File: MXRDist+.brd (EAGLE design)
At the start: 100 x 80 mm, 31 parts, among them IC1 LM741P

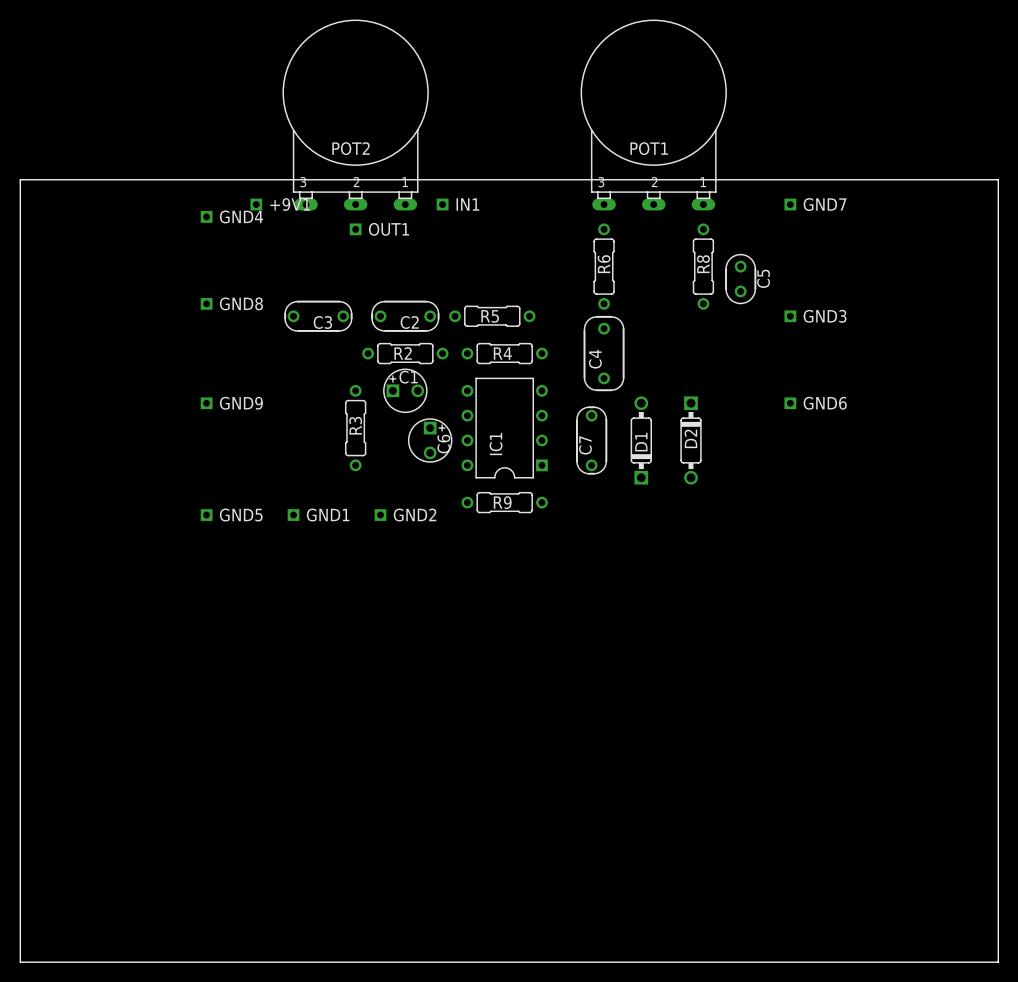
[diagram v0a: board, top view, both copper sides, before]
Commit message: New layout with diode switch
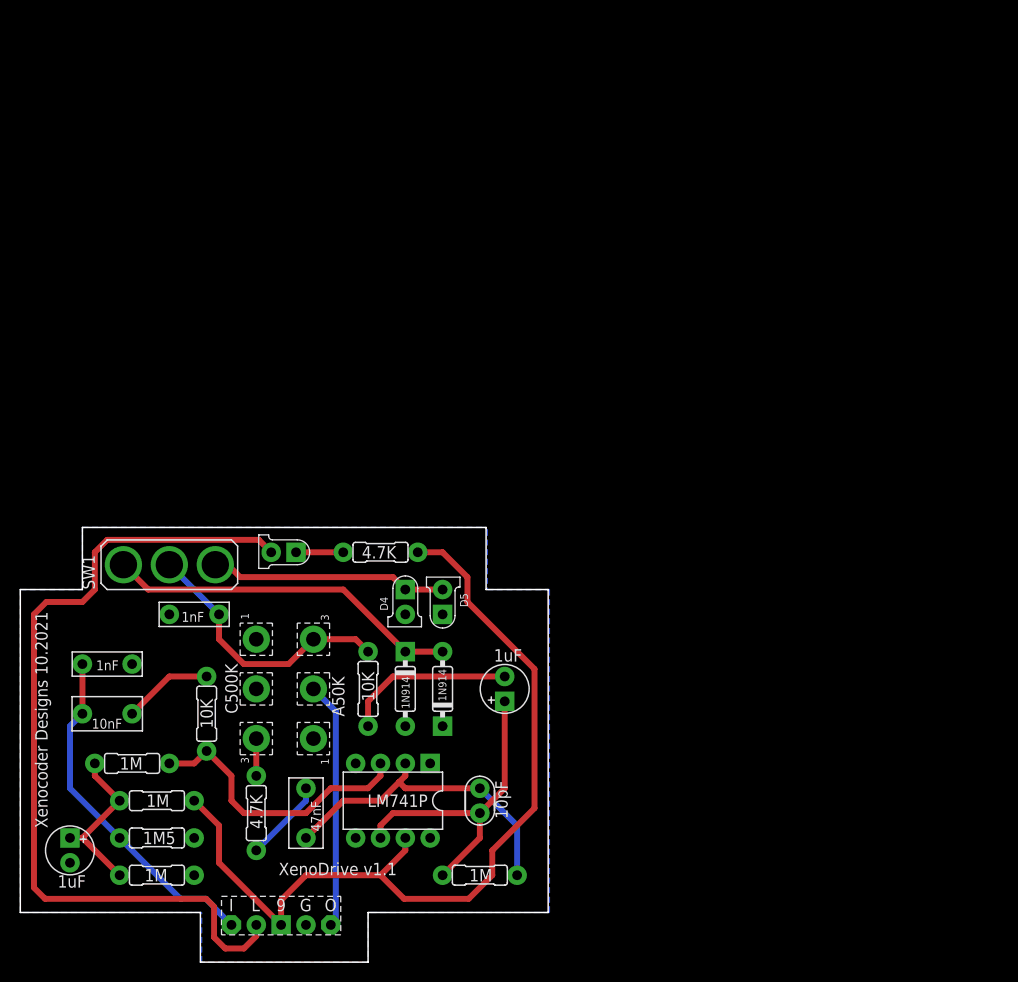
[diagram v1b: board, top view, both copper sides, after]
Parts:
- removed +9V1: +9V(T), gm-supply:SQUARE
- removed GND1, GND2, GND3, GND4, GND5, GND6, GND7, GND8, GND9: GND(T), gm-supply:SQUARE
- removed IN1: IN(T), gm-supply:SQUARE
- removed OUT1: OUT(T), gm-supply:SQUARE
- added D3: LED, mb_diodes:LED3MM
- added D4, D5: LED3MM, mb_diodes:LED3MM
- added R1: 1M5, mb_resistors:R0207/3
- added R7: 4.7K, mb_resistors:R0207/3
- added SW1: (no value), mb_switches:M9040P
- added U$1: BOARDLINK, xc_library:BOARDLINK
- C1, C6: device gm-caps-tant:044A -> mb_caps-electro:050_020_1
- C2: value 0.01uF -> 10nF; device gm-caps-film-chicklet:070X030 -> mb_caps-box:072X035
- C3, C7: value 0.001uF -> 1nF; device gm-caps-film-chicklet:070X030 -> mb_caps-box:072X025
- C4: value 0.047uF -> 47nF; device gm-caps-film-chicklet:075X040 -> mb_caps-box:072X035
- C5: device gm-caps-ceramic:050X030_025 -> mb_caps-ceramic:050X030_050_1
- D1, D2: value 1N914.3 -> 1N914; device gm-diodes:DO35-3 -> mb_diodes:DO35-3
- IC1: device gm-ics:DIL08 -> mb_ics:DIL08
- POT1, POT2: device gm-pots:16MM -> mb_pots:16MM
- R2, R3, R4, R5, R6, R8, R9: device gm-resistors:R0207/3 -> mb_resistors:R0207/3
- moved R8 66.3 mm to (47.0, 8.89), turned to 180 degrees
- moved R6 66.2 mm to (24.1, 15.2)
- moved POT1 64.1 mm to (24.1, 27.9), turned to 90 degrees
- moved C5 59.6 mm to (47.0, 16.5)
- moved C1 58.2 mm to (5.08, 11.4), turned to 270 degrees
- moved R4 56.6 mm to (11.4, 20.3)
- moved C4 56.0 mm to (29.2, 15.2)
- moved R2 52.3 mm to (14.0, 16.5), turned to 180 degrees
- moved C2 50.8 mm to (8.89, 25.4)
- moved R5 50.0 mm to (19.1, 25.4), turned to 270 degrees
- moved R3 50.0 mm to (14.0, 8.89), turned to 0 degrees
- moved POT2 49.7 mm to (30.0, 27.9), turned to 270 degrees
- moved C7 44.4 mm to (17.8, 35.6), turned to 180 degrees
- moved C3 41.6 mm to (8.89, 30.5), turned to 0 degrees
- moved IC1 39.8 mm to (38.1, 16.5), turned to 180 degrees
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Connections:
- removed net +9V: +9V1.1, IC1.7, R2.1
- removed net IN: C2.2, C3.1, IN1.1
- removed net OUT: OUT1.1, POT2.2
- new net N$10: IC1.7, R2.1, R7.2, U$1.3
- new net N$11: C2.2, C3.1, R1.2, U$1.1
- new net N$12: D3.A, R7.1
- new net N$13: D3.K, U$1.2
- new net N$14: POT2.2, U$1.5
- new net N$15: D4.A, D5.K, SW1.3
- new net N$16: D1.C, D2.A, SW1.1
- net GND: now also C1.-, D4.K, D5.A, R1.1, U$1.4; no longer C1.2, GND1.1, GND2.1, GND3.1, GND4.1, GND5.1, GND6.1, GND7.1, GND8.1, GND9.1
- net N$1: now also C1.+; no longer C1.1
- net N$5: now also C6.+; no longer C6.1
- net N$8: now also C6.-; no longer C6.2
- net N$9: now also SW1.2; no longer D1.C, D2.A
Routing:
- net N$10: track 0.00 -> 89.7 mm
- net N$13: track 0.00 -> 86.9 mm
- net N$16: track 0.00 -> 36.3 mm
- net N$11: track 0.00 -> 35.6 mm
- net N$7: track 0.00 -> 33.0 mm
- net N$5: track 0.00 -> 32.4 mm
- net N$2: track 0.00 -> 29.1 mm
- net N$9: track 0.00 -> 27.6 mm
- net N$14: track 0.00 -> 25.3 mm
- net N$15: track 0.00 -> 24.3 mm
- net N$8: track 0.00 -> 17.6 mm
- net N$1: track 0.00 -> 16.9 mm
- net N$3: track 0.00 -> 9.20 mm
- net N$6: track 0.00 -> 8.45 mm
- net N$12: track 0.00 -> 4.83 mm
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- added copper zone on layer 16, net GND
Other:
- board size 100 x 80 mm -> 54 x 44.5 mm
- board text added: "XenoDrive v1.1"
- board text added: "Xenocoder Designs 10.2021"
